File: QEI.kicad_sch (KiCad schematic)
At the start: 21 parts, among them J17 Conn_01x05_Pin, J18 Conn_01x05_Pin, J19 Conn_01x05_Pin

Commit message: update servo output
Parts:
- R38, R39, R40, R41: footprint (none) -> Resistor_SMD:R_0201_0603Metric_Pad0.64x0.40mm_HandSolder
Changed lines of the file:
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@@
 			)
 		)
-		(property "Footprint" ""
+		(property "Footprint" "Resistor_SMD:R_0201_0603Metric_Pad0.64x0.40mm_HandSolder"
 			(at 62.992 113.03 90)
 			(effects
@@
 			)
 		)
-		(property "Footprint" ""
+		(property "Footprint" "Resistor_SMD:R_0201_0603Metric_Pad0.64x0.40mm_HandSolder"
 			(at 61.722 63.5 90)
 			(effects
@@
 			)
 		)
-		(property "Footprint" ""
+		(property "Footprint" "Resistor_SMD:R_0201_0603Metric_Pad0.64x0.40mm_HandSolder"
 			(at 62.992 102.87 90)
 			(effects
@@
 			)
 		)
-		(property "Footprint" ""
+		(property "Footprint" "Resistor_SMD:R_0201_0603Metric_Pad0.64x0.40mm_HandSolder"
 			(at 61.722 73.66 90)
 			(effects

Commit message: update
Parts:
- J17, J18, J19: footprint (none) -> Connector_PinHeader_2.54mm:PinHeader_1x05_P2.54mm_Vertical
- R10, R12, R14, R16, R20, R21, R22, R26, R27, R28, R30, R32, R5, R8: footprint (none) -> Resistor_SMD:R_0201_0603Metric_Pad0.64x0.40mm_HandSolder
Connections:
- net +5V renamed 5V
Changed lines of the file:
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@@
+		)
+	)
+	(global_label "5V"
+		(shape input)
+		(at 54.61 20.32 90)
+		(fields_autoplaced yes)
+		(effects
+			(font
+				(size 1.27 1.27)
+			)
+			(justify left)
+		)
+		(property "Intersheetrefs" "${INTERSHEET_REFS}"
+			(at 54.61 15.0367 90)
+			(effects
+				(font
+					(size 1.27 1.27)
+				)
+				(justify left)
+				(hide yes)
+			)
 		)
 	)
@@
 		)
 	)
+	(global_label "5V"
+		(shape input)
+		(at 57.15 97.79 90)
+		(fields_autoplaced yes)
+		(effects
+			(font
+				(size 1.27 1.27)
+			)
+			(justify left)
+		)
+		(property "Intersheetrefs" "${INTERSHEET_REFS}"
+			(at 57.15 92.5067 90)
+			(effects
+				(font
+					(size 1.27 1.27)
+				)
+				(justify left)
+				(hide yes)
+			)
+		)
+	)
 	(global_label "QEI_3_B"
 		(shape input)
@@
 		)
 	)
+	(global_label "5V"
+		(shape input)
+		(at 55.88 58.42 90)
+		(fields_autoplaced yes)
+		(effects
+			(font
+				(size 1.27 1.27)
+			)
+			(justify left)
+		)
+		(property "Intersheetrefs" "${INTERSHEET_REFS}"
+			(at 55.88 53.1367 90)
+			(effects
+				(font
+					(size 1.27 1.27)
+				)
+				(justify left)
+				(hide yes)
+			)
+		)
+	)
 	(global_label "QEI_3_A"
 		(shape input)
@@
 			)
 		)
-		(property "Footprint" ""
+		(property "Footprint" "Connector_PinHeader_2.54mm:PinHeader_1x05_P2.54mm_Vertical"
 			(at 86.36 113.03 0)
 			(effects
@@
 			)
 		)
-		(property "Footprint" ""
+		(property "Footprint" "Resistor_SMD:R_0201_0603Metric_Pad0.64x0.40mm_HandSolder"
 			(at 36.322 33.02 90)
 			(effects
@@
 			)
 		)
-		(property "Footprint" ""
+		(property "Footprint" "Resistor_SMD:R_0201_0603Metric_Pad0.64x0.40mm_HandSolder"
 			(at 36.322 43.18 90)
 			(effects
@@
 			)
 		)
-		(property "Footprint" ""
+		(property "Footprint" "Resistor_SMD:R_0201_0603Metric_Pad0.64x0.40mm_HandSolder"
 			(at 49.022 29.21 90)
 			(effects
@@
 			)
 		)
-		(property "Footprint" ""
+		(property "Footprint" "Resistor_SMD:R_0201_0603Metric_Pad0.64x0.40mm_HandSolder"
 			(at 37.592 71.12 90)
 			(effects
@@
 			)
 		)
-		(property "Footprint" ""
+		(property "Footprint" "Resistor_SMD:R_0201_0603Metric_Pad0.64x0.40mm_HandSolder"
 			(at 60.452 35.56 90)
 			(effects
@@
 			)
 		)
-		(property "Footprint" ""
+		(property "Footprint" "Resistor_SMD:R_0201_0603Metric_Pad0.64x0.40mm_HandSolder"
 			(at 38.862 110.49 90)
 			(effects
@@
 			)
 		)
-		(property "Footprint" ""
+		(property "Footprint" "Resistor_SMD:R_0201_0603Metric_Pad0.64x0.40mm_HandSolder"
 			(at 50.292 78.74 90)
 			(effects
@@
 			)
 		)
-		(property "Footprint" ""
+		(property "Footprint" "Resistor_SMD:R_0201_0603Metric_Pad0.64x0.40mm_HandSolder"
 			(at 38.862 120.65 90)
 			(effects
@@
 				(path "/20c56496-71e7-4272-aa93-980e4fc2cc62/6bdddb73-c09b-445f-8632-feb7ee02138e"
 					(reference "R16")
-					(unit 1)
-				)
-			)
-		)
-	)
-	(symbol
-		(lib_id "power:+5V")
-		(at 57.15 97.79 0)
-		(unit 1)
-		(exclude_from_sim no)
-		(in_bom yes)
-		(on_board yes)
-		(dnp no)
-		(property "Reference" "#PWR033"
-			(at 57.15 101.6 0)
-			(effects
-				(font
-					(size 1.27 1.27)
-				)
-				(hide yes)
-			)
-		)
-		(property "Value" "+5V"
-			(at 57.15 94.234 0)
-			(effects
-				(font
-					(size 1.27 1.27)
-				)
-			)
-		)
-		(property "Footprint" ""
-			(at 57.15 97.79 0)
-			(effects
-				(font
-					(size 1.27 1.27)
-				)
-				(hide yes)
-			)
-		)
-		(property "Datasheet" ""
-			(at 57.15 97.79 0)
-			(effects
-				(font
-					(size 1.27 1.27)
-				)
-				(hide yes)
-			)
-		)
-		(property "Description" "Power symbol creates a global label with name \"+5V\""
-			(at 57.15 97.79 0)
-			(effects
-				(font
-					(size 1.27 1.27)
-				)
-				(hide yes)
-			)
-		)
-		(pin "1"
-		)
-		(instances
-			(project "carte_mere"
-				(path "/20c56496-71e7-4272-aa93-980e4fc2cc62/6bdddb73-c09b-445f-8632-feb7ee02138e"
-					(reference "#PWR033")
 					(unit 1)
 				)
@@
 			)
 		)
-		(property "Footprint" ""
+		(property "Footprint" "Connector_PinHeader_2.54mm:PinHeader_1x05_P2.54mm_Vertical"
 			(at 83.82 35.56 0)
 			(effects
@@
 			)
 		)
-		(property "Footprint" ""
+		(property "Footprint" "Resistor_SMD:R_0201_0603Metric_Pad0.64x0.40mm_HandSolder"
 			(at 51.562 118.11 90)
 			(effects
@@
 			)
 		)
-		(property "Footprint" ""
+		(property "Footprint" "Resistor_SMD:R_0201_0603Metric_Pad0.64x0.40mm_HandSolder"
 			(at 37.592 81.28 90)
 			(effects
@@
 	)
 	(symbol
-		(lib_id "power:+5V")
-		(at 54.61 20.32 0)
-		(unit 1)
-		(exclude_from_sim no)
-		(in_bom yes)
-		(on_board yes)
-		(dnp no)
-		(property "Reference" "#PWR029"
-			(at 54.61 24.13 0)
-			(effects
-				(font
-					(size 1.27 1.27)
-				)
-				(hide yes)
-			)
-		)
-		(property "Value" "+5V"
-			(at 54.61 16.764 0)
-			(effects
-				(font
-					(size 1.27 1.27)
-				)
-			)
-		)
-		(property "Footprint" ""
-			(at 54.61 20.32 0)
-			(effects
-				(font
-					(size 1.27 1.27)
-				)
-				(hide yes)
-			)
-		)
-		(property "Datasheet" ""
-			(at 54.61 20.32 0)
-			(effects
-				(font
-					(size 1.27 1.27)
-				)
-				(hide yes)
-			)
-		)
-		(property "Description" "Power symbol creates a global label with name \"+5V\""
-			(at 54.61 20.32 0)
-			(effects
-				(font
-					(size 1.27 1.27)
-				)
-				(hide yes)
-			)
-		)
-		(pin "1"
-		)
-		(instances
-			(project "carte_mere"
-				(path "/20c56496-71e7-4272-aa93-980e4fc2cc62/6bdddb73-c09b-445f-8632-feb7ee02138e"
-					(reference "#PWR029")
-					(unit 1)
-				)
-			)
-		)
-	)
-	(symbol
 		(lib_id "Device:R")
 		(at 53.34 106.68 0)
@@
 			)
 		)
-		(property "Footprint" ""
+		(property "Footprint" "Resistor_SMD:R_0201_0603Metric_Pad0.64x0.40mm_HandSolder"
 			(at 51.562 106.68 90)
 			(effects
@@
 			)
 		)
-		(property "Footprint" ""
+		(property "Footprint" "Connector_PinHeader_2.54mm:PinHeader_1x05_P2.54mm_Vertical"
 			(at 85.09 73.66 0)
 			(effects
@@
 			)
 		)
-		(property "Footprint" ""
+		(property "Footprint" "Resistor_SMD:R_0201_0603Metric_Pad0.64x0.40mm_HandSolder"
 			(at 49.022 40.64 90)
 			(effects
@@
 			)
 		)
-		(property "Footprint" ""
+		(property "Footprint" "Resistor_SMD:R_0201_0603Metric_Pad0.64x0.40mm_HandSolder"
 			(at 50.292 67.31 90)
 			(effects
@@
 	)
 	(symbol
-		(lib_id "power:+5V")
-		(at 55.88 58.42 0)
-		(unit 1)
-		(exclude_from_sim no)
-		(in_bom yes)
-		(on_board yes)
-		(dnp no)
-		(property "Reference" "#PWR031"
-			(at 55.88 62.23 0)
-			(effects
-				(font
-					(size 1.27 1.27)
-				)
-				(hide yes)
-			)
-		)
-		(property "Value" "+5V"
-			(at 55.88 54.864 0)
-			(effects
-				(font
-					(size 1.27 1.27)
-				)
-			)
-		)
-		(property "Footprint" ""
-			(at 55.88 58.42 0)
-			(effects
-				(font
-					(size 1.27 1.27)
-				)
-				(hide yes)
-			)
-		)
-		(property "Datasheet" ""
-			(at 55.88 58.42 0)
-			(effects
-				(font
-					(size 1.27 1.27)
-				)
-				(hide yes)
-			)
-		)
-		(property "Description" "Power symbol creates a global label with name \"+5V\""
-			(at 55.88 58.42 0)
-			(effects
-				(font
-					(size 1.27 1.27)
-				)
-				(hide yes)
-			)
-		)
-		(pin "1"
-		)
-		(instances
-			(project "carte_mere"
-				(path "/20c56496-71e7-4272-aa93-980e4fc2cc62/6bdddb73-c09b-445f-8632-feb7ee02138e"
-					(reference "#PWR031")
-					(unit 1)
-				)
-			)
-		)
-	)
-	(symbol
 		(lib_id "Device:R")
 		(at 62.23 25.4 0)
@@
 			)
 		)
-		(property "Footprint" ""
+		(property "Footprint" "Resistor_SMD:R_0201_0603Metric_Pad0.64x0.40mm_HandSolder"
 			(at 60.452 25.4 90)
 			(effects

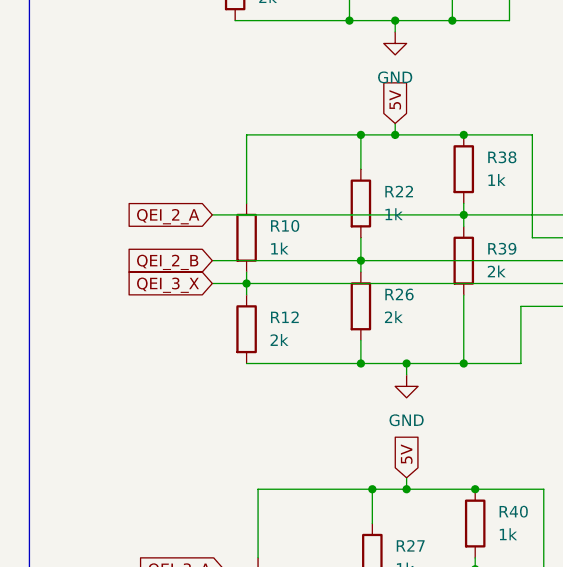
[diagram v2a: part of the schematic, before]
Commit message: v1 - need to change resistor package
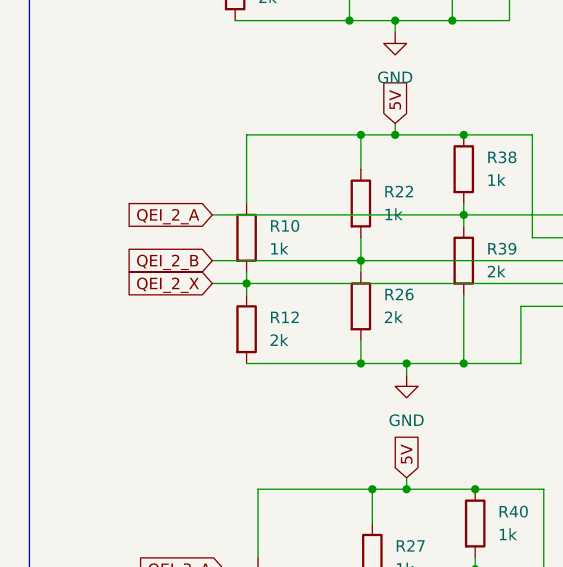
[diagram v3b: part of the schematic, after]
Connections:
- net QEI_3_X: no longer J18.4 (Pin_4), R10.2, R12.1
- new net QEI_2_X: J18.4 (Pin_4), R10.2, R12.1
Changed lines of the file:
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@@
 		)
 	)
-	(global_label "QEI_3_X"
+	(global_label "QEI_2_X"
 		(shape input)
 		(at 35.56 76.2 180)

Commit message: fix resistor and add schematic in pdf
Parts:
- R10, R12, R14, R16, R20, R21, R22, R26, R27, R28, R30, R32, R38, R39, R40, R41, R5, R8: footprint Resistor_SMD:R_0201_0603Metric_Pad0.64x0.40mm_HandSolder -> Resistor_SMD:R_0402_1005Metric
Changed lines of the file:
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@@
 			)
 		)
-		(property "Footprint" "Resistor_SMD:R_0201_0603Metric_Pad0.64x0.40mm_HandSolder"
+		(property "Footprint" "Resistor_SMD:R_0402_1005Metric"
 			(at 36.322 33.02 90)
 			(effects
@@
 			)
 		)
-		(property "Footprint" "Resistor_SMD:R_0201_0603Metric_Pad0.64x0.40mm_HandSolder"
+		(property "Footprint" "Resistor_SMD:R_0402_1005Metric"
 			(at 36.322 43.18 90)
 			(effects
@@
 			)
 		)
-		(property "Footprint" "Resistor_SMD:R_0201_0603Metric_Pad0.64x0.40mm_HandSolder"
+		(property "Footprint" "Resistor_SMD:R_0402_1005Metric"
 			(at 49.022 29.21 90)
 			(effects
@@
 			)
 		)
-		(property "Footprint" "Resistor_SMD:R_0201_0603Metric_Pad0.64x0.40mm_HandSolder"
+		(property "Footprint" "Resistor_SMD:R_0402_1005Metric"
 			(at 37.592 71.12 90)
 			(effects
@@
 			)
 		)
-		(property "Footprint" "Resistor_SMD:R_0201_0603Metric_Pad0.64x0.40mm_HandSolder"
+		(property "Footprint" "Resistor_SMD:R_0402_1005Metric"
 			(at 60.452 35.56 90)
 			(effects
@@
 			)
 		)
-		(property "Footprint" "Resistor_SMD:R_0201_0603Metric_Pad0.64x0.40mm_HandSolder"
+		(property "Footprint" "Resistor_SMD:R_0402_1005Metric"
 			(at 62.992 113.03 90)
 			(effects
@@
 			)
 		)
-		(property "Footprint" "Resistor_SMD:R_0201_0603Metric_Pad0.64x0.40mm_HandSolder"
+		(property "Footprint" "Resistor_SMD:R_0402_1005Metric"
 			(at 38.862 110.49 90)
 			(effects
@@
 			)
 		)
-		(property "Footprint" "Resistor_SMD:R_0201_0603Metric_Pad0.64x0.40mm_HandSolder"
+		(property "Footprint" "Resistor_SMD:R_0402_1005Metric"
 			(at 50.292 78.74 90)
 			(effects
@@
 			)
 		)
-		(property "Footprint" "Resistor_SMD:R_0201_0603Metric_Pad0.64x0.40mm_HandSolder"
+		(property "Footprint" "Resistor_SMD:R_0402_1005Metric"
 			(at 38.862 120.65 90)
 			(effects
@@
 			)
 		)
-		(property "Footprint" "Resistor_SMD:R_0201_0603Metric_Pad0.64x0.40mm_HandSolder"
+		(property "Footprint" "Resistor_SMD:R_0402_1005Metric"
 			(at 61.722 63.5 90)
 			(effects
@@
 			)
 		)
-		(property "Footprint" "Resistor_SMD:R_0201_0603Metric_Pad0.64x0.40mm_HandSolder"
+		(property "Footprint" "Resistor_SMD:R_0402_1005Metric"
 			(at 51.562 118.11 90)
 			(effects
@@
 			)
 		)
-		(property "Footprint" "Resistor_SMD:R_0201_0603Metric_Pad0.64x0.40mm_HandSolder"
+		(property "Footprint" "Resistor_SMD:R_0402_1005Metric"
 			(at 37.592 81.28 90)
 			(effects
@@
 			)
 		)
-		(property "Footprint" "Resistor_SMD:R_0201_0603Metric_Pad0.64x0.40mm_HandSolder"
+		(property "Footprint" "Resistor_SMD:R_0402_1005Metric"
 			(at 51.562 106.68 90)
 			(effects
@@
 			)
 		)
-		(property "Footprint" "Resistor_SMD:R_0201_0603Metric_Pad0.64x0.40mm_HandSolder"
+		(property "Footprint" "Resistor_SMD:R_0402_1005Metric"
 			(at 62.992 102.87 90)
 			(effects
@@
 			)
 		)
-		(property "Footprint" "Resistor_SMD:R_0201_0603Metric_Pad0.64x0.40mm_HandSolder"
+		(property "Footprint" "Resistor_SMD:R_0402_1005Metric"
 			(at 49.022 40.64 90)
 			(effects
@@
 			)
 		)
-		(property "Footprint" "Resistor_SMD:R_0201_0603Metric_Pad0.64x0.40mm_HandSolder"
+		(property "Footprint" "Resistor_SMD:R_0402_1005Metric"
 			(at 50.292 67.31 90)
 			(effects
@@
 			)
 		)
-		(property "Footprint" "Resistor_SMD:R_0201_0603Metric_Pad0.64x0.40mm_HandSolder"
+		(property "Footprint" "Resistor_SMD:R_0402_1005Metric"
 			(at 60.452 25.4 90)
 			(effects
@@
 			)
 		)
-		(property "Footprint" "Resistor_SMD:R_0201_0603Metric_Pad0.64x0.40mm_HandSolder"
+		(property "Footprint" "Resistor_SMD:R_0402_1005Metric"
 			(at 61.722 73.66 90)
 			(effects

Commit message: fix issues
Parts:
- removed J18, J19: Conn_01x05_Pin, Connector_PinHeader_2.54mm:PinHeader_1x05_P2.54mm_Vertical, symbol Connector:Conn_01x05_Pin
- removed R10, R22, R30, R38: 1k, Resistor_SMD:R_0402_1005Metric, symbol Device:R
- removed R12, R26, R32, R39, R41: 2k, Resistor_SMD:R_0402_1005Metric, symbol Device:R
- added C1, C2, C23, C24, C25, C26, C27, C28, C29: 100nF, Capacitor_SMD:C_0402_1005Metric, symbol Device:C
- added J39, J40: Conn_01x05_Pin, Connector_PinHeader_2.54mm:PinHeader_1x05_P2.54mm_Vertical, symbol Connector:Conn_01x05_Pin
- added U10, U11, U12, U13, U3, U4, U7, U8, U9: SN74LV1T34DCK, Package_TO_SOT_SMD:SOT-353_SC-70-5, symbol Logic_LevelTranslator:SN74LV1T34DCK
- R14, R20, R27, R40, R5: footprint Resistor_SMD:R_0402_1005Metric -> Capacitor_SMD:C_0402_1005Metric
- R16, R21, R28, R8: value 2k -> 1k; footprint Resistor_SMD:R_0402_1005Metric -> Capacitor_SMD:C_0402_1005Metric
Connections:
- net 5V: now also J39.2 (Pin_2), J40.2 (Pin_2); no longer R14.1, R20.1, R27.1, R40.1, R5.1
- net GND: now also C1.1, C2.1, C23.1, C24.1, C25.1, C26.1, C27.1, C28.1, C29.1, J39.5 (Pin_5), J40.5 (Pin_5), U10.3 (GND), U11.3 (GND), U12.3 (GND), U13.3 (GND), U3.3 (GND), U4.3 (GND), U7.3 (GND), U8.3 (GND), U9.3 (GND); no longer R16.2, R21.2, R28.2, R8.2
- net QEI_1_A: now also U3.4 (Y); no longer J17.1 (Pin_1)
- net QEI_1_B: now also U4.4 (Y); no longer J17.3 (Pin_3), R20.2, R21.1
- net QEI_1_X: now also U7.4 (Y); no longer J17.4 (Pin_4), R5.2, R8.1
- net QEI_2_A: now also U10.4 (Y)
- net QEI_2_B: now also U8.4 (Y)
- net QEI_2_X: now also U9.4 (Y)
- net QEI_3_A: now also U13.4 (Y); no longer R40.2
- net QEI_3_B: now also U11.4 (Y); no longer R27.2, R28.1
- net QEI_3_X: now also U12.4 (Y); no longer R14.2, R16.1
- new net: R14.1, U7.2 (A)
- new net: R5.1, U3.2 (A)
- new net: J17.1 (Pin_1), R5.2
- new net: R20.1, U9.2 (A)
- new net: J39.4 (Pin_4), R20.2
- new net: R8.1, U4.2 (A)
- new net: R16.1, U8.2 (A)
- new net: R40.1, U13.2 (A)
- new net: R27.1, U11.2 (A)
- new net: J40.3 (Pin_3), R27.2
- new net: J39.3 (Pin_3), R16.2
- new net: R21.1, U10.2 (A)
- new net: J40.1 (Pin_1), R40.2
- new net: J40.4 (Pin_4), R28.2
- new net: J39.1 (Pin_1), R21.2
- new net: J17.3 (Pin_3), R8.2
- new net: J17.4 (Pin_4), R14.2
- new net: R28.1, U12.2 (A)
- new net 3.3V: C1.2, C2.2, C23.2, C24.2, C25.2, C26.2, C27.2, C28.2, C29.2, U10.5 (VCC), U11.5 (VCC), U12.5 (VCC), U13.5 (VCC), U3.5 (VCC), U4.5 (VCC), U7.5 (VCC), U8.5 (VCC), U9.5 (VCC)
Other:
- moved on the sheet: J17

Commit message: update
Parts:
- J17, J39, J40: now left out of the parts list
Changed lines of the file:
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@@
 		(unit 1)
 		(exclude_from_sim no)
-		(in_bom yes)
+		(in_bom no)
 		(on_board yes)
 		(dnp no)
@@
 		(unit 1)
 		(exclude_from_sim no)
-		(in_bom yes)
+		(in_bom no)
 		(on_board yes)
 		(dnp no)
@@
 		(unit 1)
 		(exclude_from_sim no)
-		(in_bom yes)
-		(on_board yes)
-		(dnp no)
+		(in_bom no)
+		(on_board yes)
+		(dnp no)
